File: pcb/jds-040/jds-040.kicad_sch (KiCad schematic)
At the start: 8 parts, among them J1 USB_C_Receptacle_USB2.0, J2 Conn_01x12_MountingPin

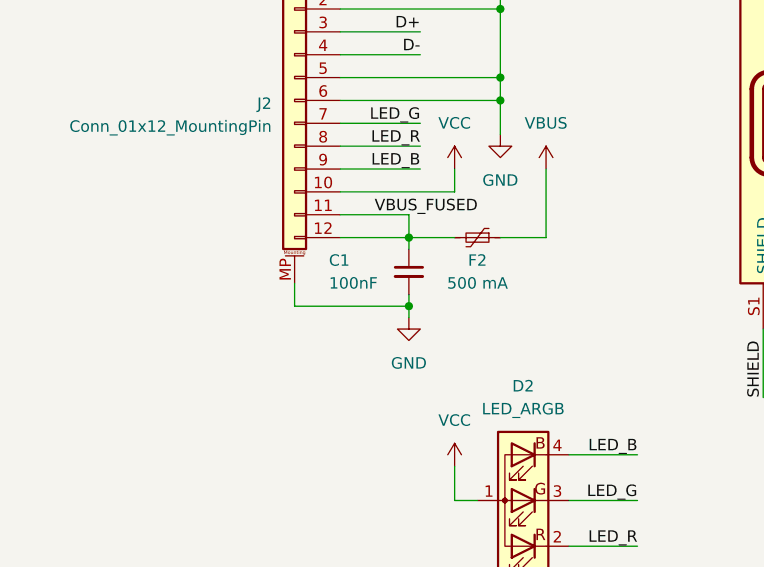
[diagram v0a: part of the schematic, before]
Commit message: Finished silkscreen, minor adjustments.
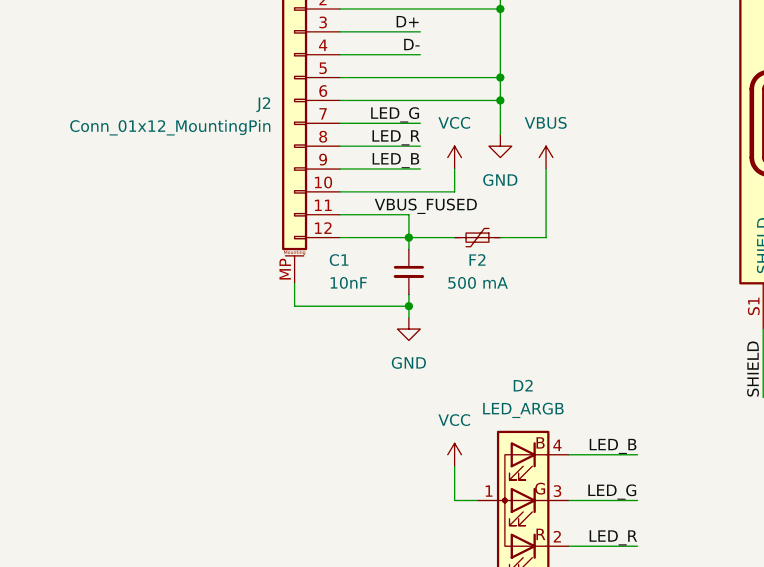
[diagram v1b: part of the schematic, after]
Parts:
- C1: value 100nF -> 10nF
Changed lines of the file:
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@@
       (effects (font (size 1.27 1.27)) (justify left))
     )
-    (property "Value" "100nF" (at 52.07 82.55 0)
+    (property "Value" "10nF" (at 52.07 82.55 0)
       (effects (font (size 1.27 1.27)) (justify left))
     )

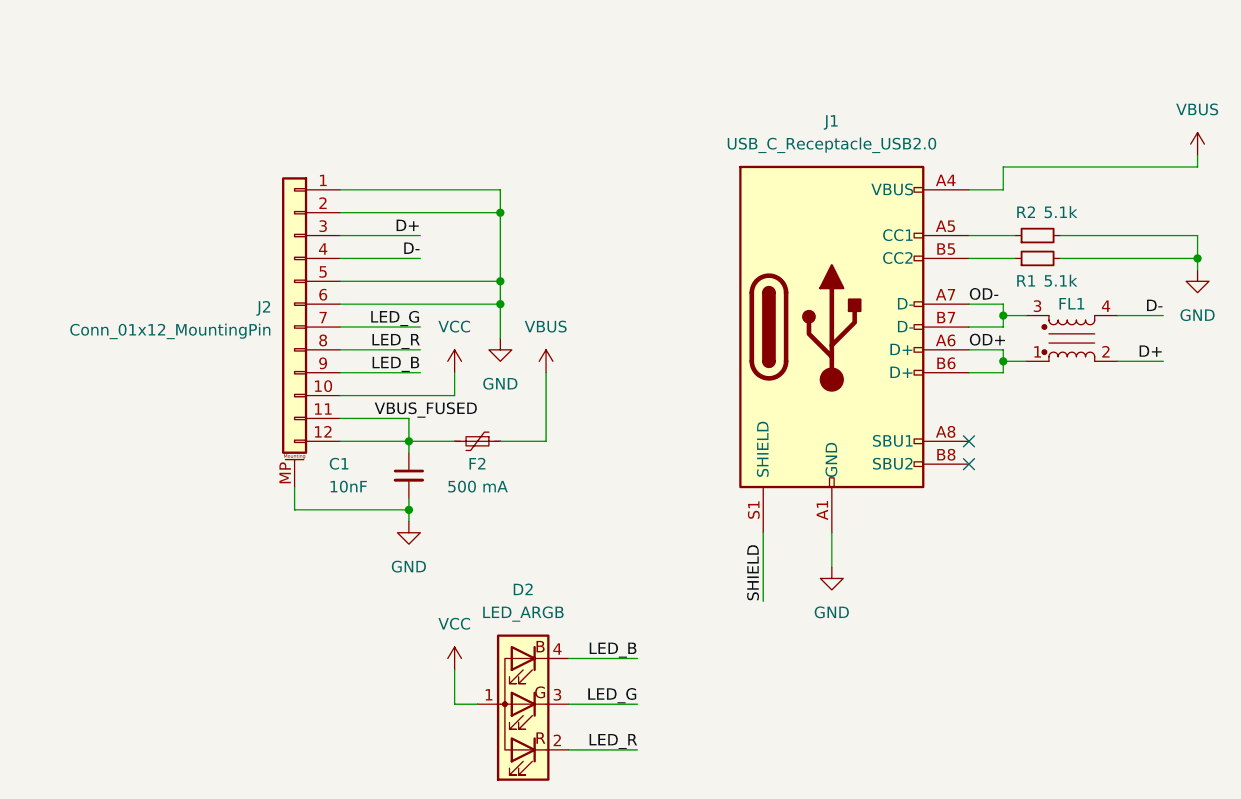
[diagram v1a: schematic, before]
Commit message: Updated sheets and component properties.
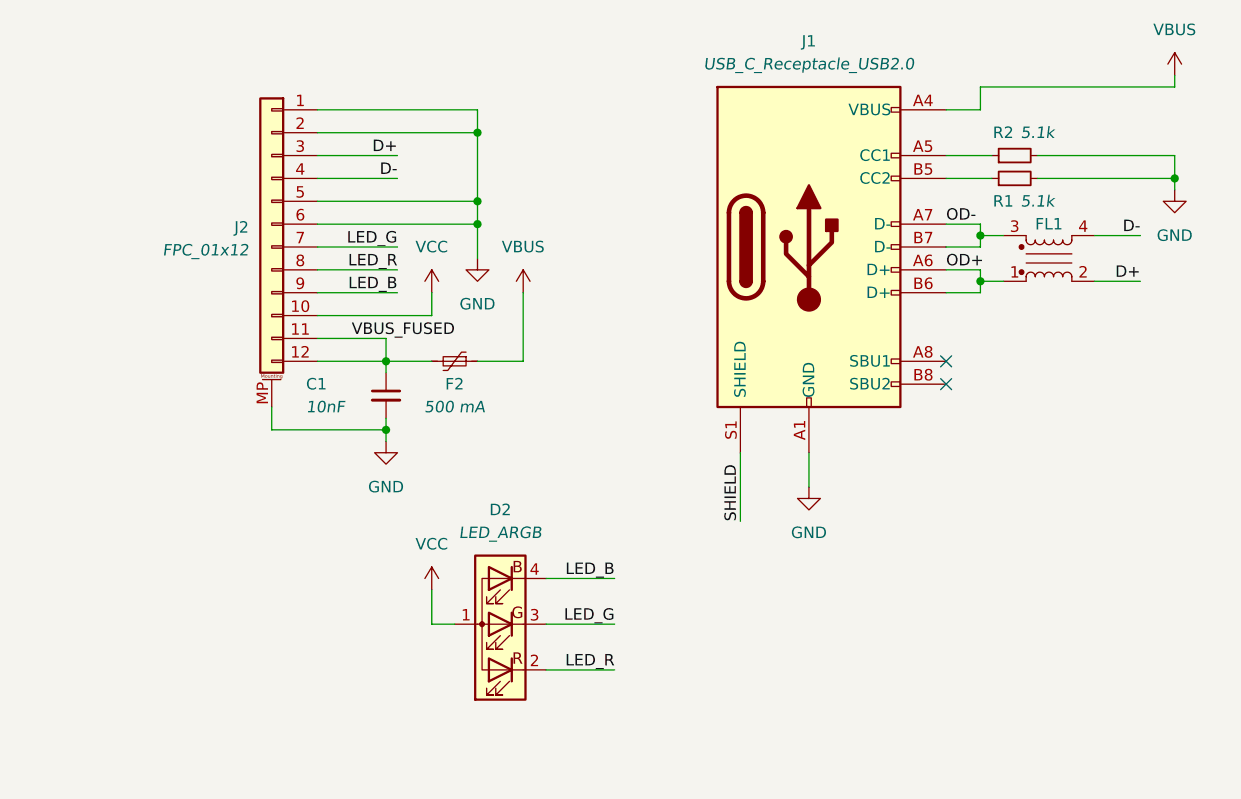
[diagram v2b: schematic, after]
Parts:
- C1: LCSC (none) -> C15195
- D2: LCSC (none) -> C727903
- F2: LCSC (none) -> C210356
- FL1: LCSC (none) -> C383353
- J1: LCSC (none) -> C963213
- J2: value Conn_01x12_MountingPin -> FPC_01x12; LCSC (none) -> C466532
- R1, R2: LCSC (none) -> C105872
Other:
- company: (none) -> Petr Moucha
- title: (none) -> USB-C Daughterboard - JDS-040
- moved on the sheet: C1, D2, F2, FL1, J1, J2, R1, R2
